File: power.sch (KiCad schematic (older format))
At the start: 15 parts

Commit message: Se hace cambios en el esquematico y se anexa PCB
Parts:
- C201, C202, C203, C204: renamed from C?; footprint (none) -> Capacitor_SMD:C_1206_3216Metric_Pad1.42x1.75mm_HandSolder
- D201: renamed from D?; footprint (none) -> LED_SMD:LED_0805_2012Metric_Pad1.15x1.40mm_HandSolder
- J201: renamed from J?; footprint (none) -> Connector_BarrelJack:BarrelJack_CUI_PJ-102AH_Horizontal
- L201, L202, L203, L204, L205: renamed from L?; footprint (none) -> Inductor_SMD:L_1206_3216Metric_Pad1.42x1.75mm_HandSolder
- R201: renamed from R?; footprint (none) -> Resistor_SMD:R_0805_2012Metric_Pad1.15x1.40mm_HandSolder
- SW201: renamed from SW?; footprint (none) -> Button_Switch_SMD:SW_SPST_EVQPE1
- U202: renamed from U?; footprint (none) -> Package_TO_SOT_SMD:TO-263-3_TabPin2
- gave numbers to parts that had none: 1
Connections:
- net PW5V: now also C203.1, U202.3 (VI)
- net PW12V renamed PW12
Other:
- moved on the sheet: L201, L202, L203, L204, L205

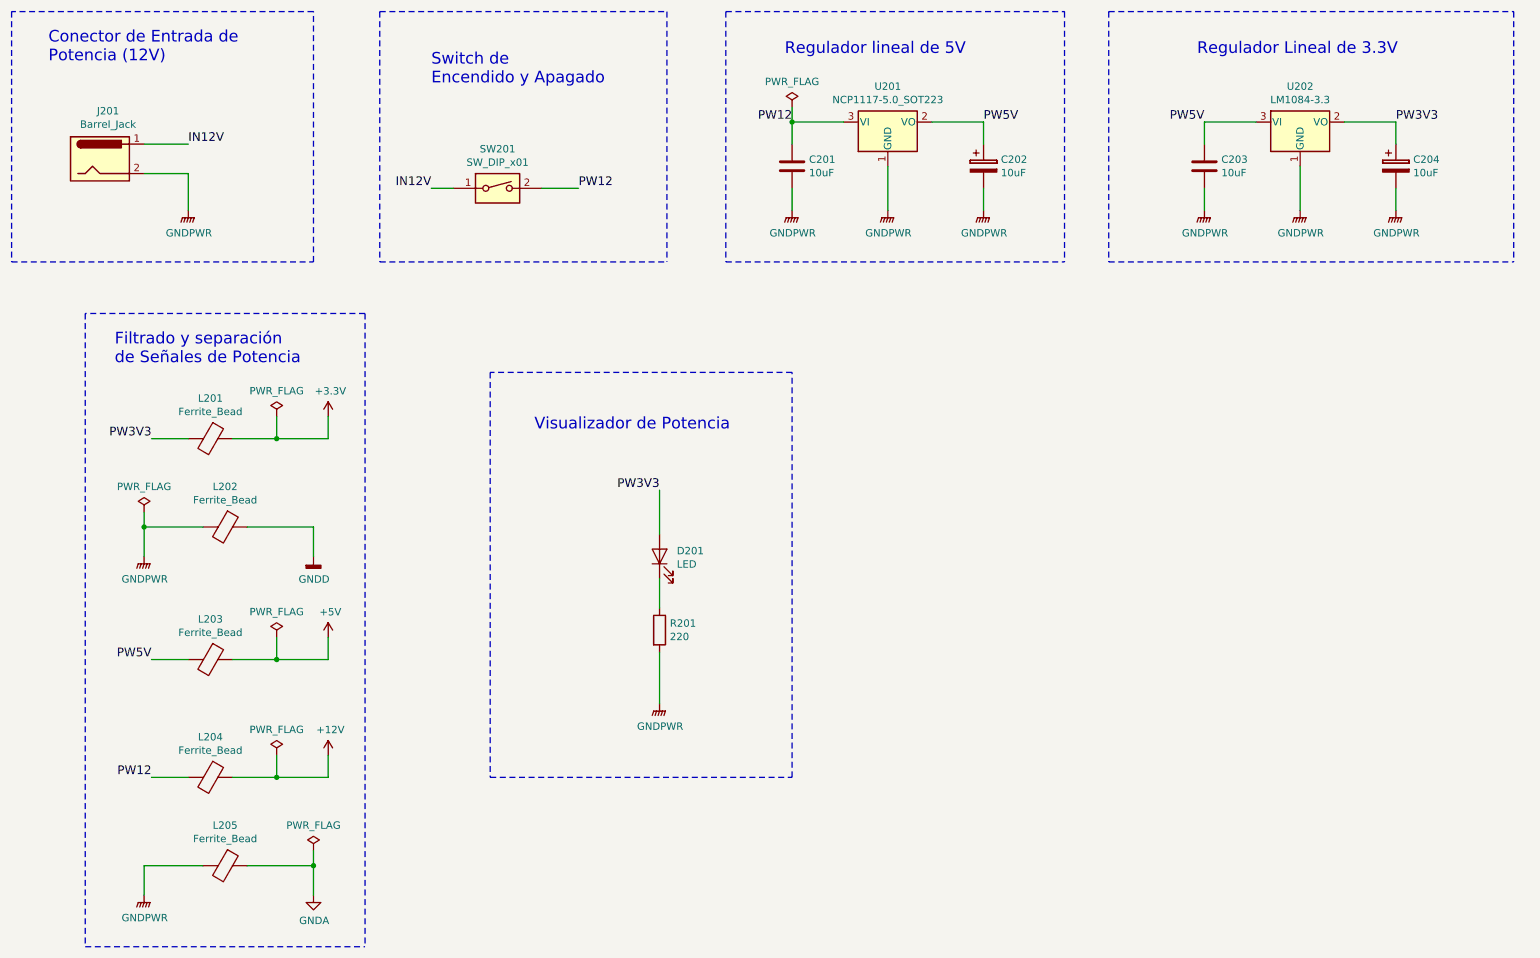
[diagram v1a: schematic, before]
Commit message: Se realizan correcciones finales y se agregan carpetas BOM, Datasheet, Doc, Gerbers, lib.pretty y shapes3D
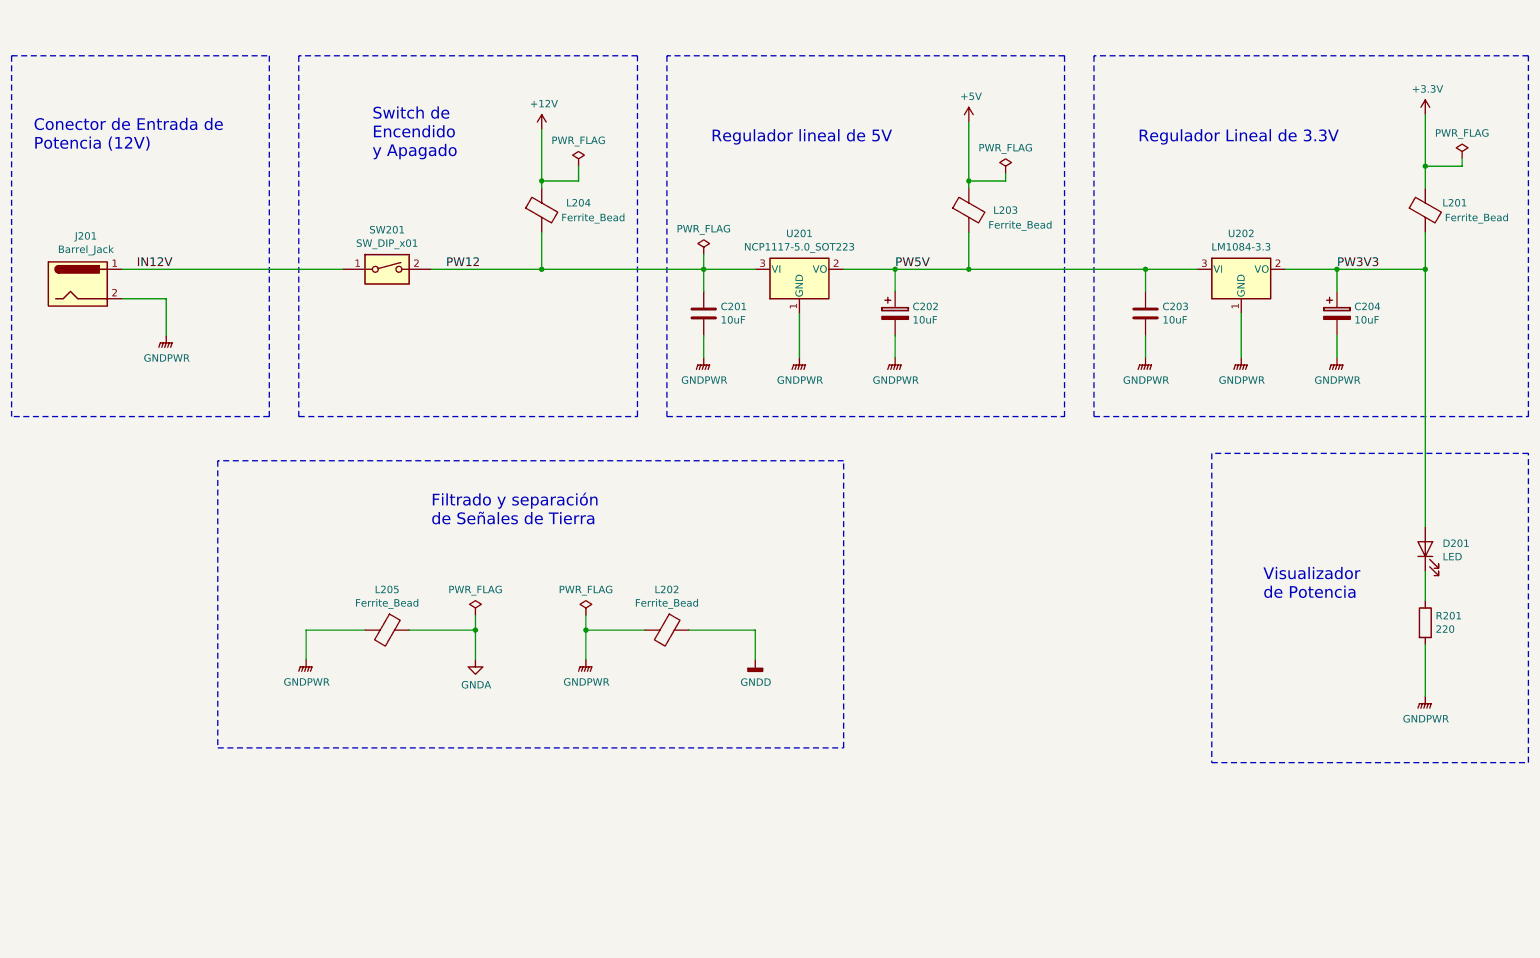
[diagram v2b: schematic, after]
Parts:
- J201: footprint Connector_BarrelJack:BarrelJack_CUI_PJ-102AH_Horizontal -> Connector_BarrelJack:BarrelJack_CUI_PJ-063AH_Horizontal
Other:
- note added: "Filtrado y separación \nde Señales de Tierra"
- note added: "Switch de \nEncendido \ny Apagado"
- note added: "Visualizador \nde Potencia"
- note removed: "Filtrado y separación \nde Señales de Potencia"
- note removed: "Switch de \nEncendido y Apagado"
- note removed: "Visualizador de Potencia"
- moved on the sheet: C201, C202, C203, C204, D201, J201, L201, L202, L203, L204, L205, R201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
